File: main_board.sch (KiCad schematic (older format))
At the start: 49 parts, among them J104 HEADER_2, J105 HEADER_4, J106 HEADER_2, J107 HEADER_4x2, J108 HEADER_6, M101 MOUNTING-HOLE, M102 MOUNTING-HOLE, M103 MOUNTING-HOLE, M104 MOUNTING-HOLE, M105 MOUNTING-HOLE, SW101 SPST, SW102 SPST, SW103 SPST, SW104 SPST, SW105 SPST, SW106 SPST, SW107 SPST, SW108 SPST, SW109 SPST, SW110 SPST, SW111 SPST, SW112 SPST, SW113 SPST, SW114 SPST, SW115 SPST, SW116 SPST, SW117 SPST, SW118 SPST, SW119 SPST, SW120 SPST, SW121 SPST, SW122 SPST, SW123 SPST, SW124 SPST, SW125 SPST, SW126 SPST, SW127 SPST, SW128 SPST, U101 Teensy-LC, U102 ESP-12E

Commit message: Final main board v0.1
Last big upload commit before I start doing proper commits ;)
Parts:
- removed J107: HEADER_4x2, Socket_Strips:Socket_Strip_Straight_2x04, symbol HEADER_4x2
- added J1: HEADER_5x2, Socket_Strips:Socket_Strip_Straight_2x05, symbol HEADER_5x2
- added J2: HEADER_1, Socket_Strips:Socket_Strip_Straight_1x01, symbol HEADER_1
- added U1: ESP-01v090, ESP8266:ESP-01, symbol ESP-01v090
- J106: footprint Socket_Strips:Socket_Strip_Straight_1x02 -> w_conn_jst-ph:b2b-ph-kl
- J108: footprint Socket_Strips:Socket_Strip_Straight_1x06 -> Pin_Headers:Pin_Header_Angled_1x06
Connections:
- net FTDI_RX is gone; now on net ESP_TX: J108.5
- net +3V3: now also J1.2, U1.7 (VCC)
- net +BATT: now also J108.6; no longer J108.3
- net ESP_RX: now also J108.3, U1.8 (URXD); no longer U101.3 (1_TX1_MISO1_Touch)
- net ESP_TX: now also U1.1 (UTXD); no longer U101.2 (0_RX1_MOSI1_Touch)
- net FLEX1: now also J1.1
- net FLEX2: now also J1.3
- net FLEX3: now also J1.5
- net FLEX4: now also J1.7
- net GND: now also J1.8, U1.2 (GND)
- net I2C_SCL: now also J1.4
- net I2C_SDA: now also J1.6
- net KM_COL5: now also U101.13 (11_MOSI0); no longer U101.11 (9_RX2_PWM)
- net KM_COL6: now also U101.14 (12_MISO0); no longer U101.12 (10_TX2_CS0_PWM)
- net at R101.2, U102.1 (REST): now also U1.5 (RST)
- net at R103.2, U102.17 (GPIO2): now also U1.4 (GPIO2)
- net at R104.2, U102.18 (GPIO0): now also U1.6 (GPIO0)
- net at R102.2, U102.3 (CH_PD): now also U1.3 (CH_PD)
- net TEENSY_TX: now reaches J108.2
- net TEENSY_TX: now also U101.3 (1_TX1_MISO1_Touch)
- net FTDI_TX renamed TEENSY_RX
- net TEENSY_RX: now also U101.2 (0_RX1_MOSI1_Touch)
- new net: J1.10, J2.1
- new net BUZZER: J1.9, U101.12 (10_TX2_CS0_PWM)
- no-connect marks 21 -> 19
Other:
- moved on the sheet: D102, R101, R102, R103, R104, R105, SW101, SW102, SW103, SW104, SW105, SW106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

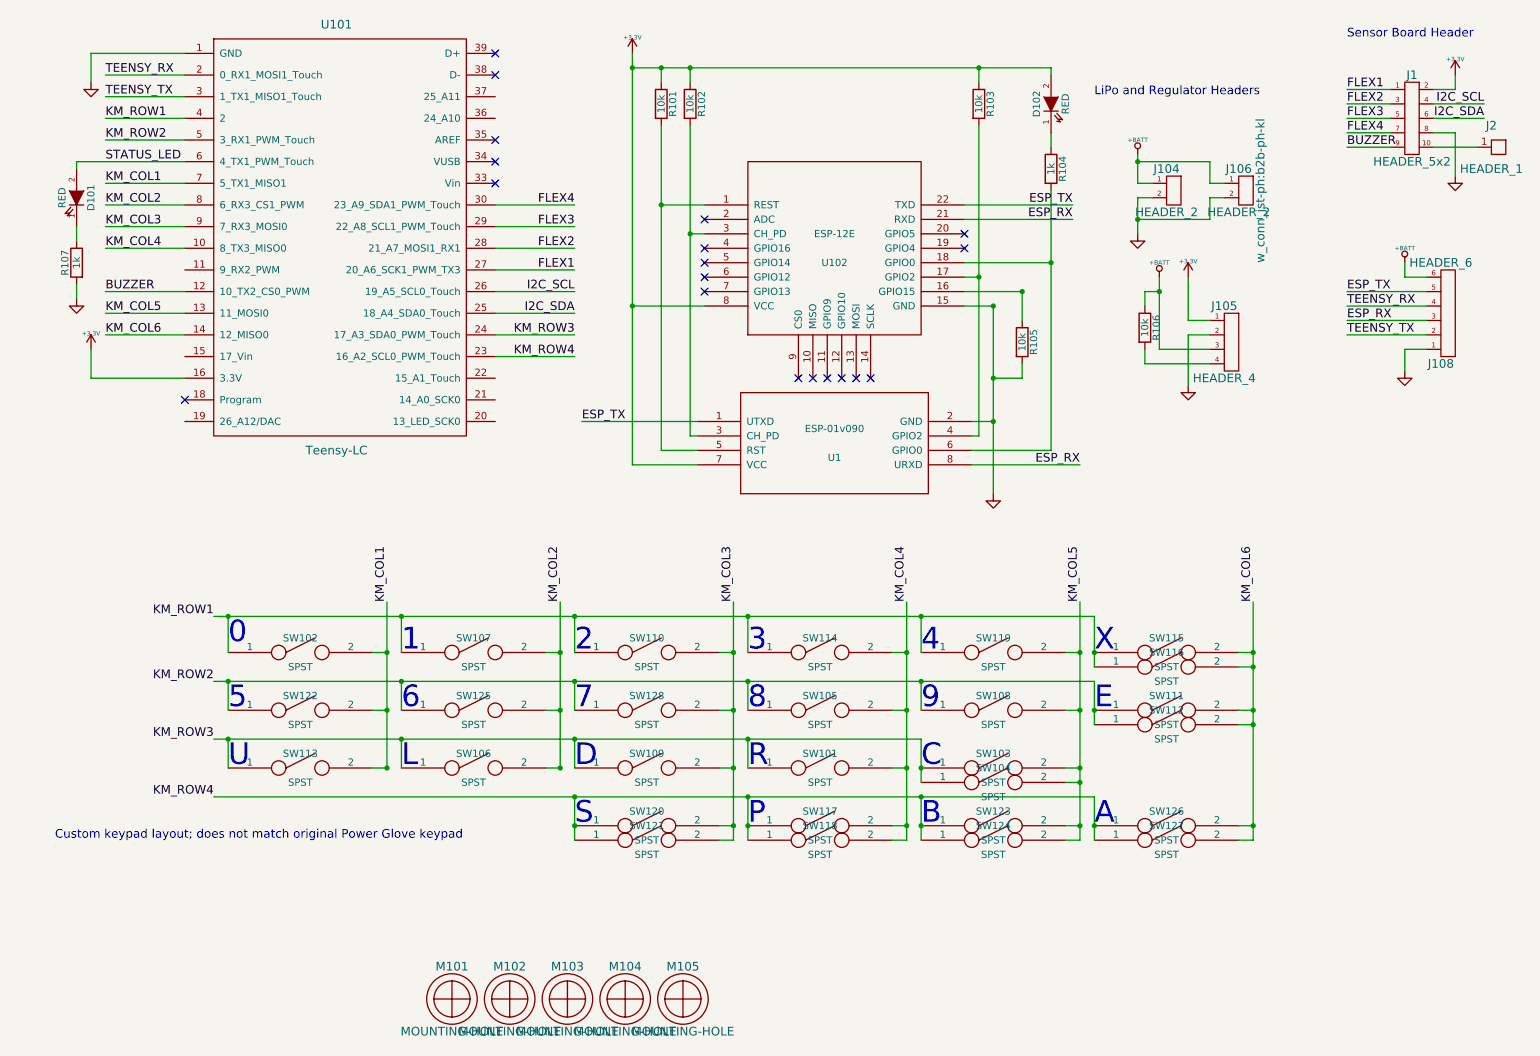
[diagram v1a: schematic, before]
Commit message: Cleaned up schematics and sensor board PCB
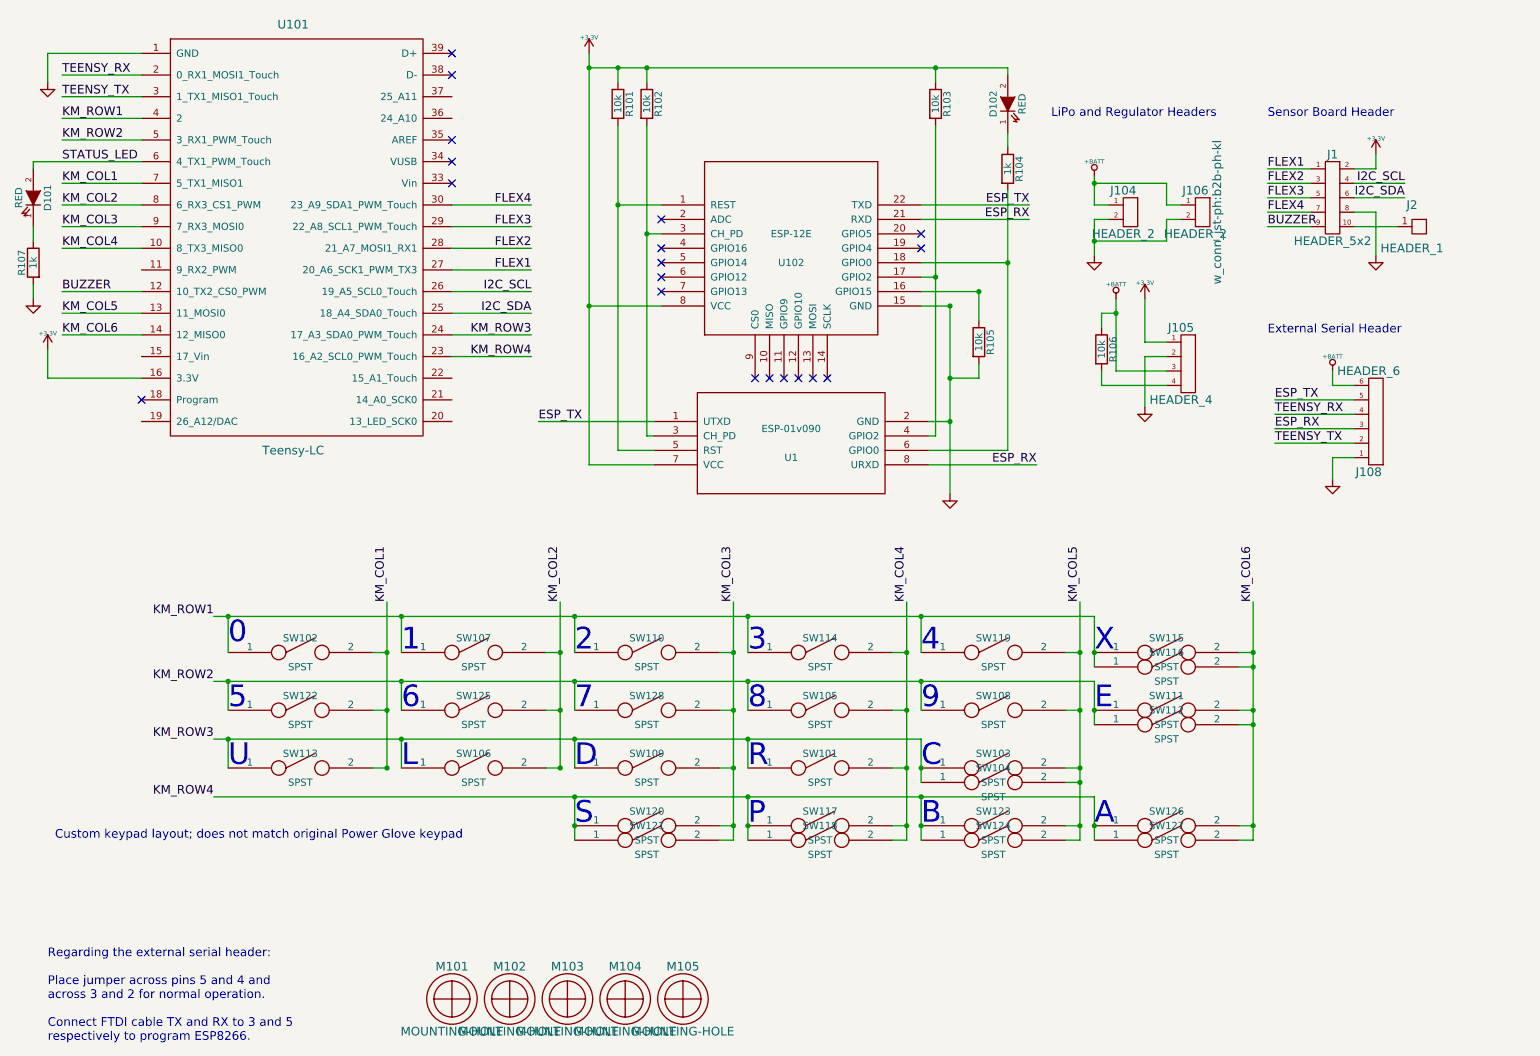
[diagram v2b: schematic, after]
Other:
- note added: "External Serial Header"
- note added: "Regarding the external serial header:\n\nPlace jumper across pins 5 and 4 and\nacross 3 and 2 for normal operation.\n\nConnect FTDI cable TX and RX to 3 and 5\nrespectively to program ESP8266."
- moved on the sheet: D101, D102, J1, J104, J105, J106, J108, J2, R101, R102, R103, R104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

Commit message: Bumped version to 0.2, cleaned schematic, added voltage divider resistors, boot and reset buttons
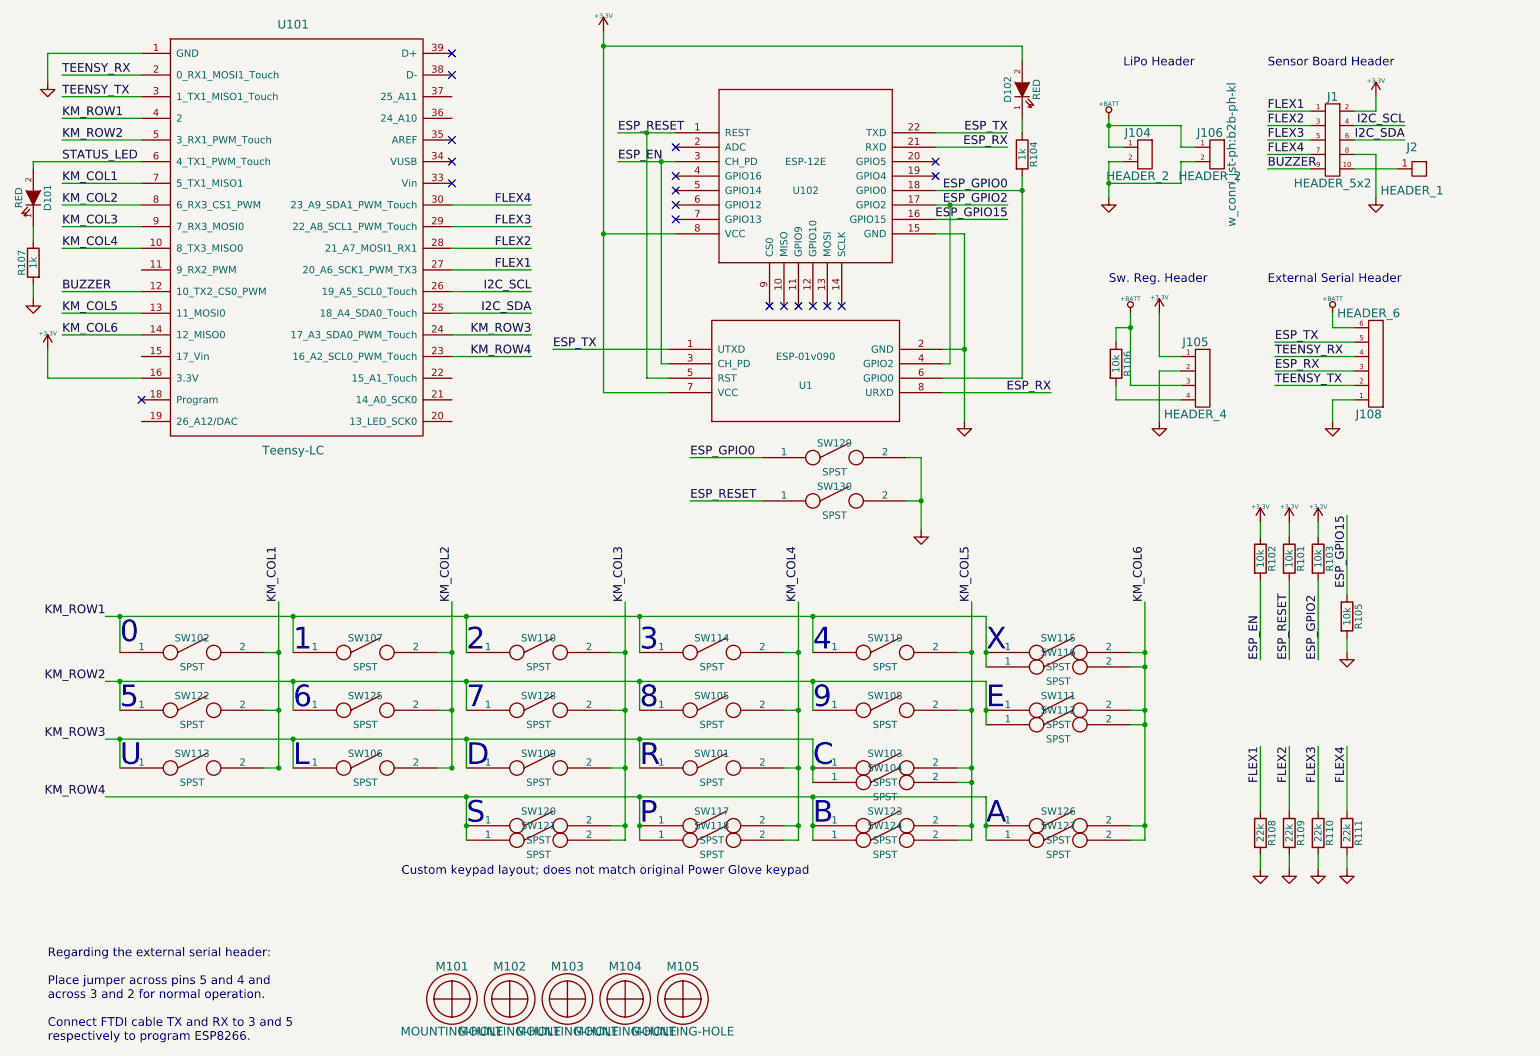
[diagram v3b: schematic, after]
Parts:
- added R108, R109, R110, R111: 22k, Resistors_SMD:R_0805, symbol R
- added SW129, SW130: SPST, Socket_Strips:Socket_Strip_Straight_1x02, symbol SPST
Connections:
- net FLEX1: now also R108.1
- net FLEX2: now also R109.1
- net FLEX3: now also R110.1
- net FLEX4: now also R111.1
- net GND: now also R108.2, R109.2, R110.2, R111.2, SW129.2, SW130.2
- net ESP_RESET: now reaches R101.2, U1.5 (RST), U102.1 (REST)
- net ESP_RESET: now also SW130.1
- net ESP_GPIO15: now reaches R105.1, U102.16 (GPIO15)
- net ESP_GPIO2: now reaches R103.2, U1.4 (GPIO2), U102.17 (GPIO2)
- net ESP_GPIO0: now reaches R104.2, U1.6 (GPIO0), U102.18 (GPIO0)
- net ESP_GPIO0: now also SW129.1
- net ESP_EN: now reaches R102.2, U1.3 (CH_PD), U102.3 (CH_PD)
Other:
- note added: "LiPo Header"
- note added: "Sw. Reg. Header"
- note removed: "LiPo and Regulator Headers"
- moved on the sheet: D102, J1, J104, J105, J106, J108, J2, R101, R102, R103, R104, R105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
